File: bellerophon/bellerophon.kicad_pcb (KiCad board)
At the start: 4 copper layers, 35 x 85 mm, 43 parts, among them Q1 ST3413A, Q2 SPP3414S23RG, Q3 SPP3414S23RG, U1 HT7350-A, U2 BNO055, U3 MPL3115A2, U4 Teensy4.0, U5 XTSD, Y1 32.768kHz

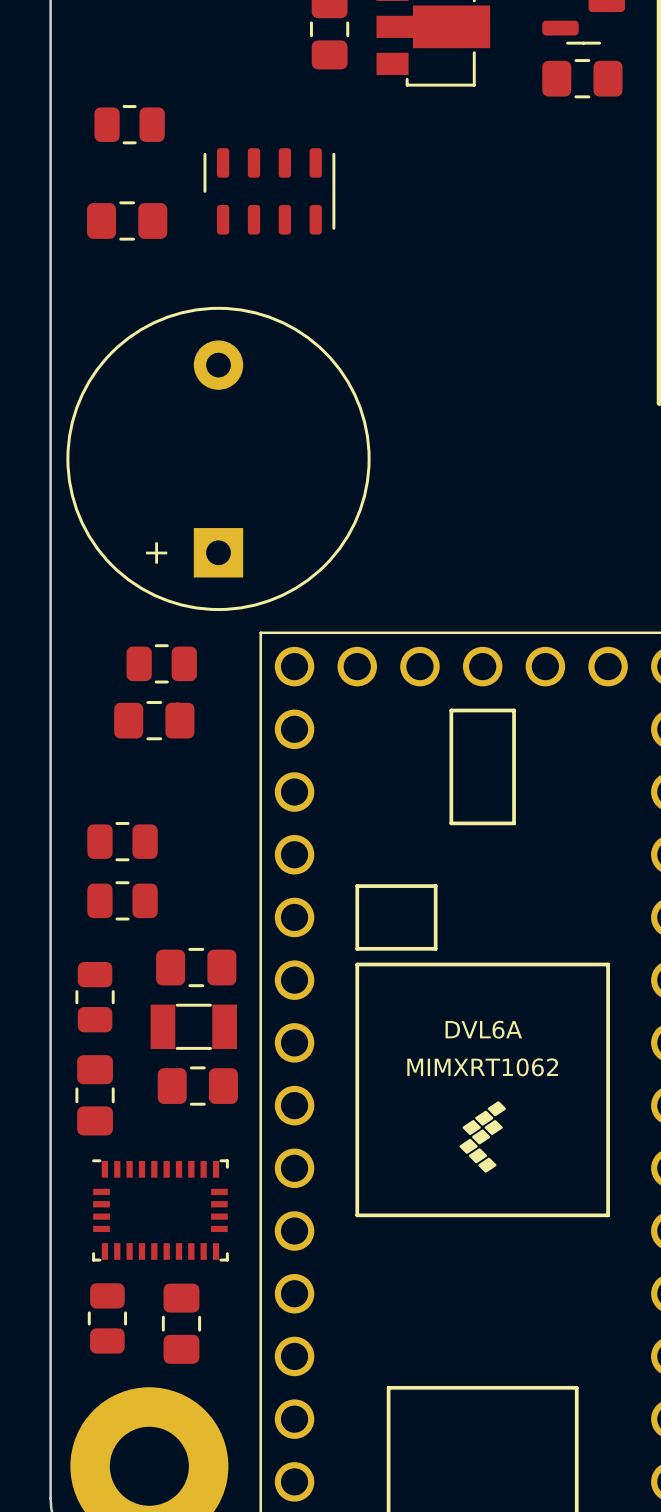
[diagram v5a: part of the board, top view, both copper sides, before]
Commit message: add back i2cADDR pin for bno055
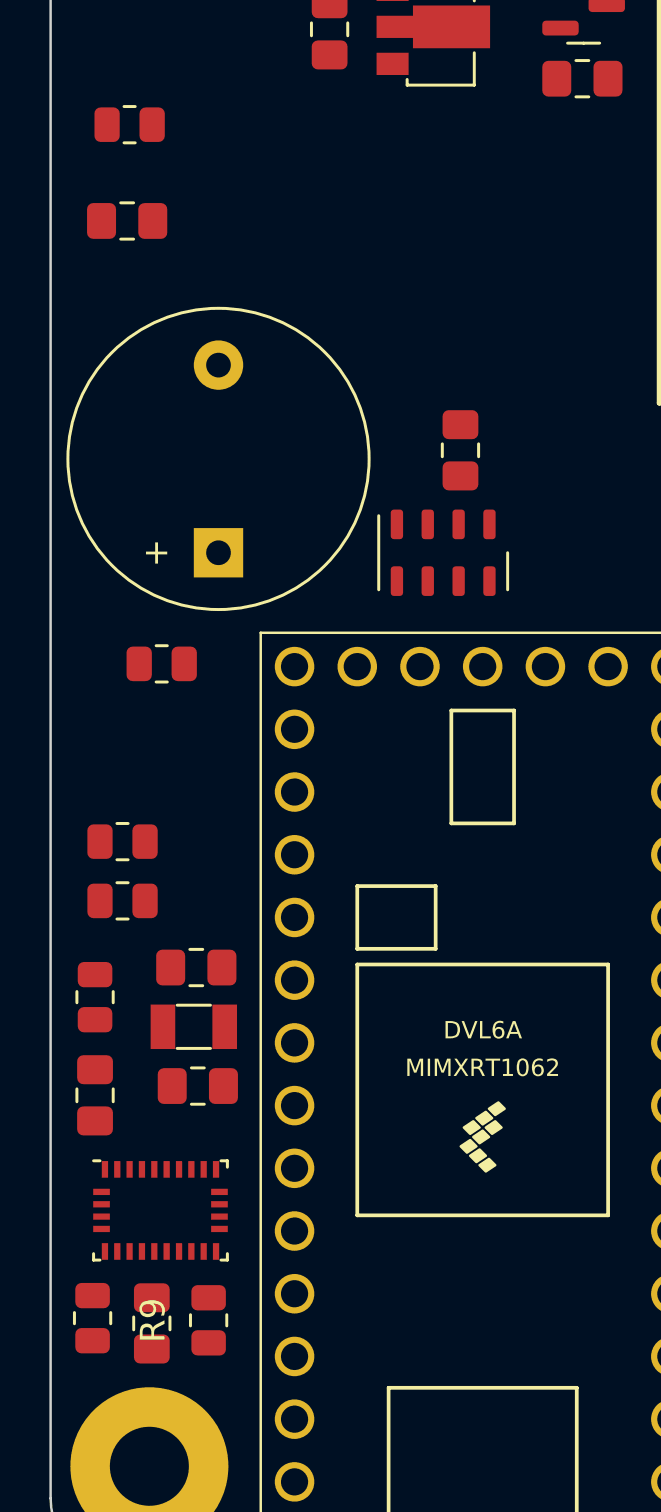
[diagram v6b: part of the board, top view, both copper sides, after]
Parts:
- added R9: 10k, Resistor_SMD:R_0805_2012Metric, F.Cu at (208.9, 134.8)
- moved C8 16.5 mm to (219.1, 99.5), turned to 90 degrees
- moved U3 16.2 mm to (218.4, 103.7), turned to -90 degrees
- moved C5 1.20 mm to (206.6, 134.9)
- moved R5 0.60 mm to (204.2, 134.7)
- renumbered R11 to R10, R12 to R11, R13 to R12, R14 to R13, R15 to R14, R16 to R15, R17 to R16, R18 to R17, R19 to R18, R20 to R19
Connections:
- U2 pad 17: unconnected-(U2-Pad17) -> /I2CADDR_3V

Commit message: finalize MPL circuitry
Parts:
- moved R6 25.9 mm to (208.3, 112.1)
- moved C6 20.3 mm to (224.0, 98.9), turned to 0 degrees
- moved U3 2.21 mm to (220.4, 102.8)
- moved C9 1.60 mm to (220.1, 98.3)
- moved R7 0.51 mm to (206.6, 108.5), turned to -90 degrees
- moved R9 0.10 mm to (208.9, 134.7)
- renumbered C7 to C8, C8 to C9
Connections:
- net Net-(C8-Pad1) renamed /CAP1
- C8 pad 1: /VDD -> +3.3V
- U2 pad 3: /VDD -> +3.3V
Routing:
- net GND: track 0.60 -> 0.00 mm

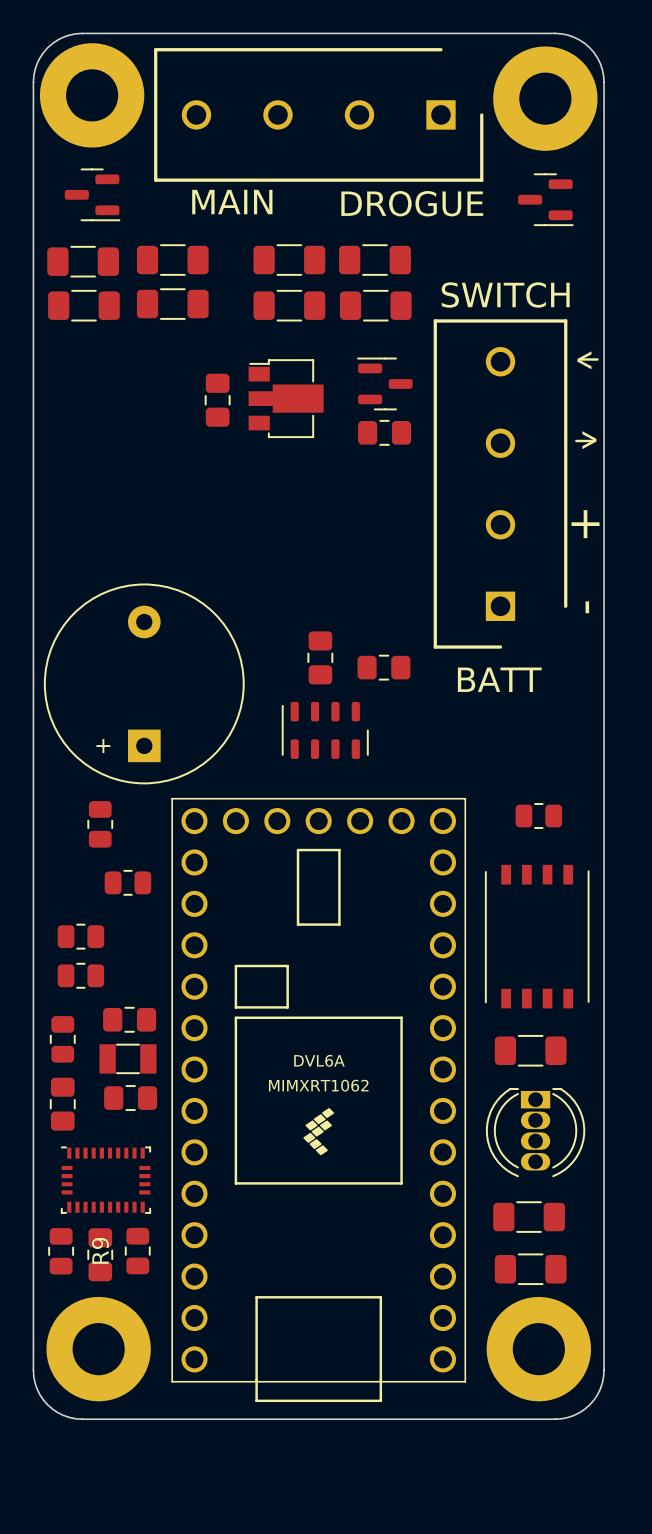
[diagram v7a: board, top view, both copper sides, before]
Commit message: reduce length to 79mm
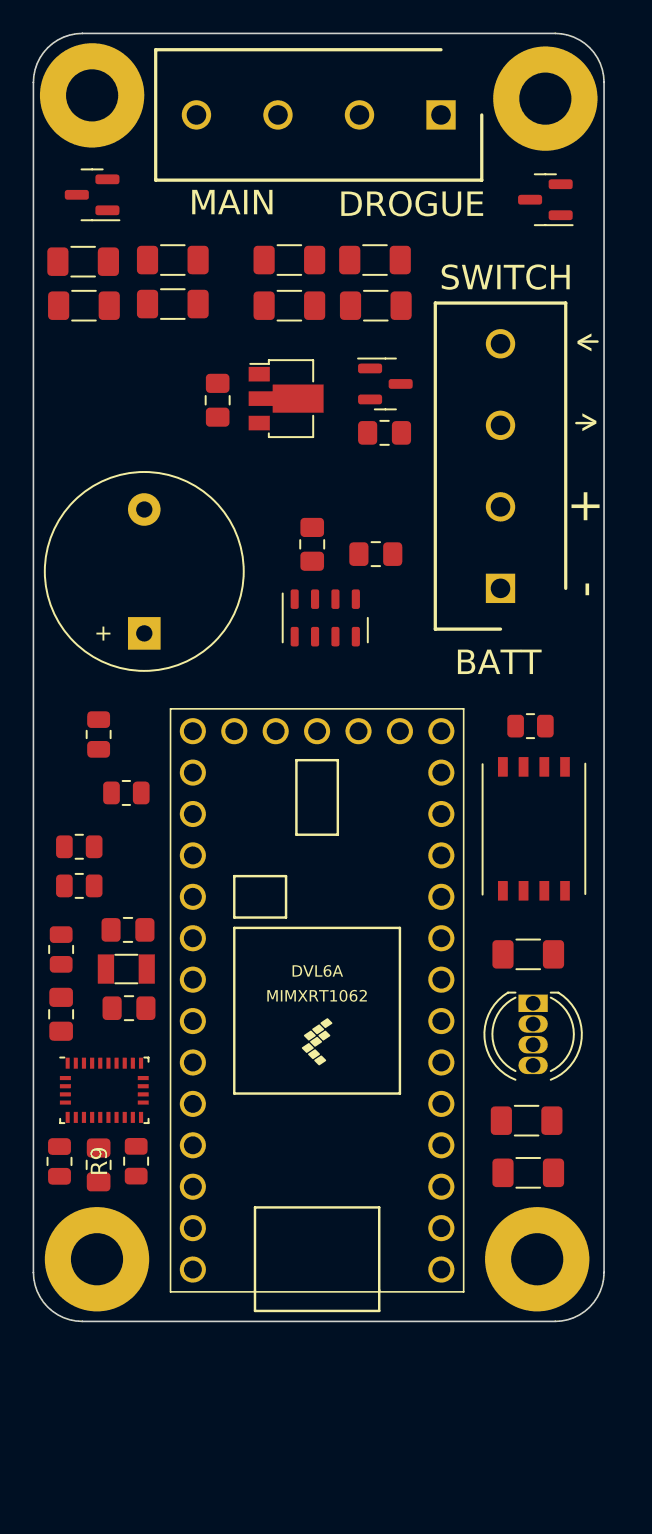
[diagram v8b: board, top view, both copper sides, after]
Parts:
- moved C6 6.98 mm to (223.5, 91.9)
- moved C9 6.98 mm to (219.6, 91.3)
- moved BZ1 6.90 mm to (209.3, 96.8)
- moved U3 6.90 mm to (220.4, 95.8)
- moved U5 6.62 mm to (233.2, 108.8)
- moved R2 5.91 mm to (232.8, 129.9)
- moved D1 5.91 mm to (233.2, 119.5)
- moved R3 5.91 mm to (232.8, 116.5)
- moved R1 5.91 mm to (232.8, 126.7)
- moved R16 5.54 mm to (233.0, 102.5)
- moved C3 5.51 mm to (208.4, 119.8)
- moved C4 5.51 mm to (208.3, 115.0)
- moved C8 5.51 mm to (204.2, 120.2)
- moved R10 5.51 mm to (205.3, 112.3)
- moved R4 5.51 mm to (204.2, 116.2)
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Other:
- board size 35 x 85 mm -> 35 x 79 mm
